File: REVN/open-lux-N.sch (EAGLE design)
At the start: 71 parts, among them IC2 MCP73831, IC3 ATMEGA32U4-AU, IC4 MCP1700-33, J2 EG1206, Q1 BSS123, Q4 BSS123, T1 FDN340P, T2 FDN340P, X2 USBSMD, X3 8MHz

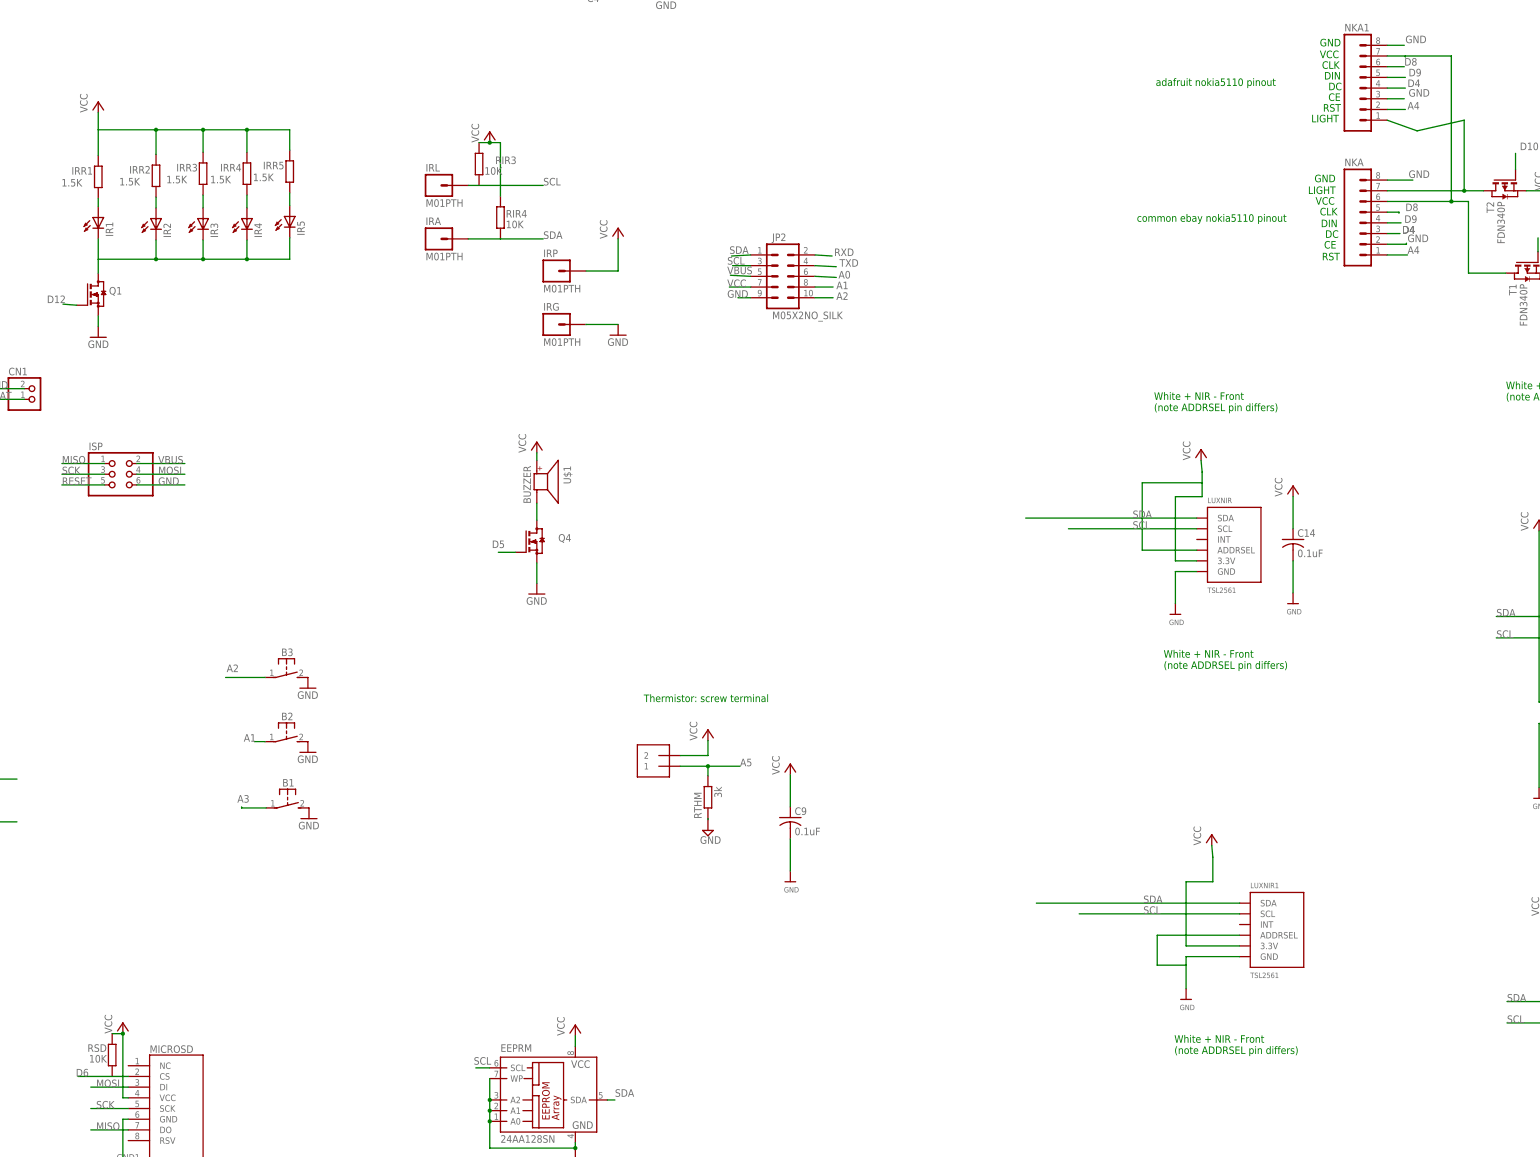
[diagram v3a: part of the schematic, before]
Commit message: fully routed
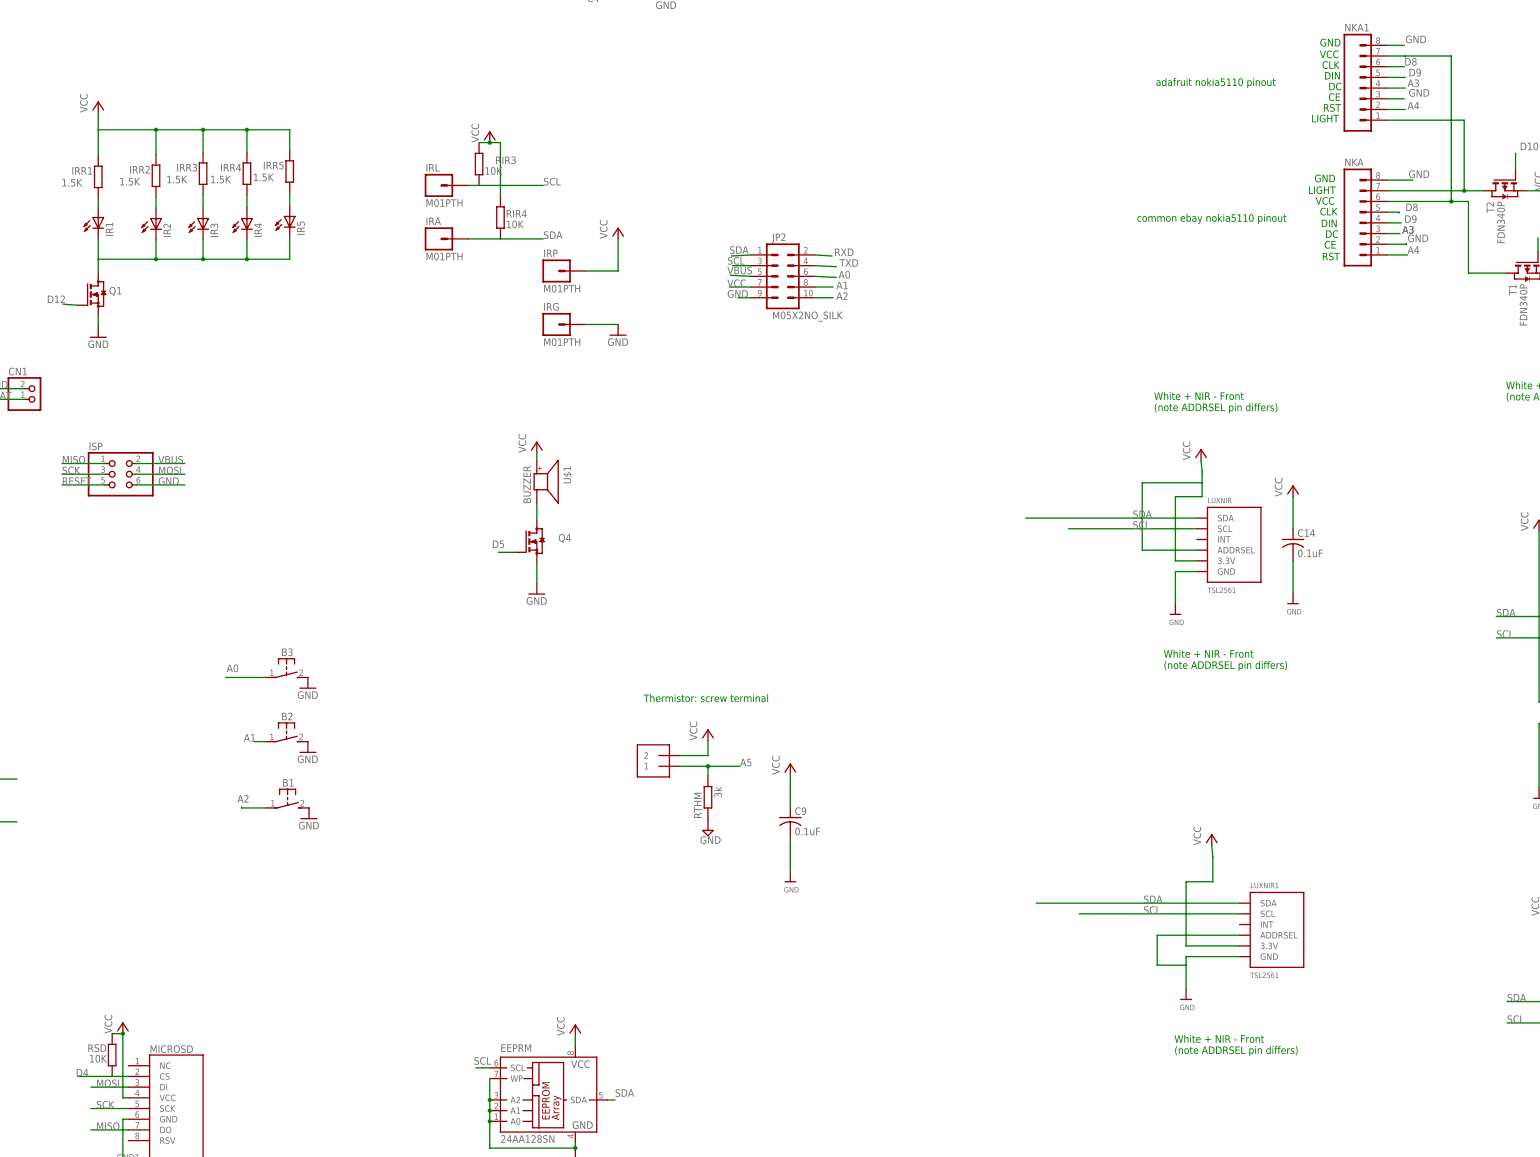
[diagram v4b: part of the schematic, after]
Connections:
- net A0: now also B3.P
- net A2: now also B1.P; no longer B3.P
- net A3: now also NKA.3, NKA1.4; no longer B1.P
- net D4: now also MICROSD.CS, RSD.1; no longer NKA.3, NKA1.4
- net D6: no longer MICROSD.CS, RSD.1
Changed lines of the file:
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@@
 <pinref part="JP2" gate="G$1" pin="6"/>
+</segment>
+<segment>
+<pinref part="B3" gate="1" pin="P"/>
+<wire x1="157.48" y1="25.4" x2="148.082" y2="25.4" width="0.1524" layer="91"/>
+<label x="148.336" y="26.67" size="1.778" layer="95"/>
 </segment>
 </net>
@@
 </segment>
 <segment>
-<pinref part="B3" gate="1" pin="P"/>
-<wire x1="157.48" y1="25.4" x2="148.082" y2="25.4" width="0.1524" layer="91"/>
-<label x="148.336" y="26.67" size="1.778" layer="95"/>
+<pinref part="B1" gate="1" pin="P"/>
+<wire x1="157.734" y1="-5.588" x2="151.892" y2="-5.588" width="0.1524" layer="91"/>
+<wire x1="151.892" y1="-5.588" x2="151.892" y2="-5.334" width="0.1524" layer="91"/>
+<label x="150.876" y="-4.318" size="1.778" layer="95"/>
 </segment>
 </net>
@@
 </segment>
 <segment>
-<pinref part="B1" gate="1" pin="P"/>
-<wire x1="157.734" y1="-5.588" x2="151.892" y2="-5.588" width="0.1524" layer="91"/>
-<wire x1="151.892" y1="-5.588" x2="151.892" y2="-5.334" width="0.1524" layer="91"/>
-<label x="150.876" y="-4.318" size="1.778" layer="95"/>
-</segment>
-</net>
-<net name="D4" class="0">
-<segment>
-<pinref part="IC3" gate="G$1" pin="PD4(ICP1/ADC8)"/>
-<wire x1="73.152" y1="-11.43" x2="76.708" y2="-11.43" width="0.1524" layer="91"/>
-<label x="76.962" y="-10.922" size="1.778" layer="95"/>
+<label x="428.752" y="165.608" size="1.778" layer="95"/>
+<pinref part="NKA1" gate="G$1" pin="4"/>
+<wire x1="423.926" y1="165.354" x2="428.244" y2="165.354" width="0.1524" layer="91"/>
 </segment>
 <segment>
@@
 <label x="427.482" y="130.81" size="1.778" layer="95"/>
 </segment>
-<segment>
-<label x="428.752" y="165.608" size="1.778" layer="95"/>
-<pinref part="NKA1" gate="G$1" pin="4"/>
-<wire x1="423.926" y1="165.354" x2="428.244" y2="165.354" width="0.1524" layer="91"/>
-</segment>
-</net>
-<net name="D8" class="0">
-<segment>
-<pinref part="IC3" gate="G$1" pin="PB4(ADC11)"/>
-<wire x1="73.152" y1="11.43" x2="78.994" y2="11.43" width="0.1524" layer="91"/>
-<label x="79.248" y="11.684" size="1.778" layer="95"/>
-</segment>
-<segment>
-<wire x1="423.926" y1="135.89" x2="426.72" y2="135.89" width="0.1524" layer="91"/>
-<wire x1="426.72" y1="135.89" x2="426.72" y2="135.636" width="0.1524" layer="91"/>
-<label x="428.244" y="136.144" size="1.778" layer="95"/>
-<pinref part="NKA" gate="G$1" pin="5"/>
-</segment>
-<segment>
-<pinref part="NKA1" gate="G$1" pin="6"/>
-<wire x1="423.926" y1="170.434" x2="427.99" y2="170.434" width="0.1524" layer="91"/>
-<label x="427.99" y="170.688" size="1.778" layer="95"/>
-</segment>
-</net>
-<net name="D5" class="0">
-<segment>
-<wire x1="73.152" y1="26.67" x2="80.772" y2="26.67" width="0.1524" layer="91"/>
-<label x="75.692" y="26.67" size="1.778" layer="95"/>
-<pinref part="IC3" gate="G$1" pin="PC6(OC1A)"/>
-</segment>
-<segment>
-<pinref part="Q4" gate="G$1" pin="G"/>
-<wire x1="216.916" y1="55.118" x2="212.852" y2="55.118" width="0.1524" layer="91"/>
-<label x="211.328" y="56.134" size="1.778" layer="95"/>
-</segment>
-</net>
-<net name="D6" class="0">
-<segment>
-<wire x1="85.852" y1="-3.81" x2="73.152" y2="-3.81" width="0.1524" layer="91"/>
-<label x="75.692" y="-3.81" size="1.778" layer="95"/>
-<pinref part="IC3" gate="G$1" pin="PD7(OC4D/ADC10/T0)"/>
-</segment>
-<segment>
-<pinref part="WS1" gate="G$1" pin="IN"/>
-<wire x1="252.73" y1="199.39" x2="261.366" y2="199.39" width="0.1524" layer="91"/>
-<label x="261.112" y="199.898" size="1.778" layer="95"/>
+</net>
+<net name="D4" class="0">
+<segment>
+<pinref part="IC3" gate="G$1" pin="PD4(ICP1/ADC8)"/>
+<wire x1="73.152" y1="-11.43" x2="76.708" y2="-11.43" width="0.1524" layer="91"/>
+<label x="76.962" y="-10.922" size="1.778" layer="95"/>
 </segment>
 <segment>
@@
 <wire x1="121.158" y1="-69.342" x2="113.03" y2="-69.342" width="0.1524" layer="91"/>
 <label x="112.522" y="-69.342" size="1.778" layer="95"/>
+</segment>
+</net>
+<net name="D8" class="0">
+<segment>
+<pinref part="IC3" gate="G$1" pin="PB4(ADC11)"/>
+<wire x1="73.152" y1="11.43" x2="78.994" y2="11.43" width="0.1524" layer="91"/>
+<label x="79.248" y="11.684" size="1.778" layer="95"/>
+</segment>
+<segment>
+<wire x1="423.926" y1="135.89" x2="426.72" y2="135.89" width="0.1524" layer="91"/>
+<wire x1="426.72" y1="135.89" x2="426.72" y2="135.636" width="0.1524" layer="91"/>
+<label x="428.244" y="136.144" size="1.778" layer="95"/>
+<pinref part="NKA" gate="G$1" pin="5"/>
+</segment>
+<segment>
+<pinref part="NKA1" gate="G$1" pin="6"/>
+<wire x1="423.926" y1="170.434" x2="427.99" y2="170.434" width="0.1524" layer="91"/>
+<label x="427.99" y="170.688" size="1.778" layer="95"/>
+</segment>
+</net>
+<net name="D5" class="0">
+<segment>
+<wire x1="73.152" y1="26.67" x2="80.772" y2="26.67" width="0.1524" layer="91"/>
+<label x="75.692" y="26.67" size="1.778" layer="95"/>
+<pinref part="IC3" gate="G$1" pin="PC6(OC1A)"/>
+</segment>
+<segment>
+<pinref part="Q4" gate="G$1" pin="G"/>
+<wire x1="216.916" y1="55.118" x2="212.852" y2="55.118" width="0.1524" layer="91"/>
+<label x="211.328" y="56.134" size="1.778" layer="95"/>
+</segment>
+</net>
+<net name="D6" class="0">
+<segment>
+<wire x1="85.852" y1="-3.81" x2="73.152" y2="-3.81" width="0.1524" layer="91"/>
+<label x="75.692" y="-3.81" size="1.778" layer="95"/>
+<pinref part="IC3" gate="G$1" pin="PD7(OC4D/ADC10/T0)"/>
+</segment>
+<segment>
+<pinref part="WS1" gate="G$1" pin="IN"/>
+<wire x1="252.73" y1="199.39" x2="261.366" y2="199.39" width="0.1524" layer="91"/>
+<label x="261.112" y="199.898" size="1.778" layer="95"/>
 </segment>
 </net>
@@
 <segment>
 <pinref part="NKA1" gate="G$1" pin="1"/>
-<wire x1="423.926" y1="157.734" x2="431.038" y2="155.194" width="0.1524" layer="91"/>
+<wire x1="423.926" y1="157.734" x2="442.214" y2="157.734" width="0.1524" layer="91"/>
 <wire x1="423.926" y1="140.97" x2="442.214" y2="140.97" width="0.1524" layer="91"/>
 <pinref part="T2" gate="A" pin="D"/>
 <pinref part="NKA" gate="G$1" pin="7"/>
 <wire x1="442.214" y1="140.97" x2="446.786" y2="140.97" width="0.1524" layer="91"/>
-<wire x1="431.038" y1="155.194" x2="442.214" y2="157.734" width="0.1524" layer="91"/>
 <wire x1="442.214" y1="157.734" x2="442.214" y2="140.97" width="0.1524" layer="91"/>
 <junction x="442.214" y="140.97"/>

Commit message: update
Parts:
- renumbered CN1 to JST, R-BTN to RESET
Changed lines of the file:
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@@
 <part name="RC" library="rcl" deviceset="R-EU_" device="R0805" value="22K"/>
 <part name="BAT1" library="SparkFunNew" deviceset="BATTERY" device="BATTCOM_20MM_PTH_SMT" value="LIR2032"/>
-<part name="CN1" library="adafruit" deviceset="JST_2PIN" device="-SMT-RA"/>
+<part name="JST" library="adafruit" deviceset="JST_2PIN" device="-SMT-RA"/>
 <part name="IC4" library="adafruit" deviceset="MCP1700" device="SOT233" value="MCP1700-33"/>
 <part name="C3" library="resistor" deviceset="C-EU" device="C0805" value="10u"/>
@@
 <part name="GND15" library="supply1" deviceset="GND" device=""/>
 <part name="GND16" library="supply1" deviceset="GND" device=""/>
-<part name="R-BTN" library="adafruit" deviceset="EVQQ2" device="" value=""/>
+<part name="RESET" library="adafruit" deviceset="EVQQ2" device="" value=""/>
 <part name="P+16" library="supply1" deviceset="VCC" device=""/>
 <part name="P+17" library="supply1" deviceset="VCC" device=""/>
@@
 <attribute name="VALUE" x="35.56" y="97.79" size="1.778" layer="96"/>
 </instance>
-<instance part="CN1" gate="G$1" x="102.87" y="91.44"/>
+<instance part="JST" gate="G$1" x="102.87" y="91.44"/>
 <instance part="IC4" gate="1" x="64.77" y="113.03" smashed="yes">
 <attribute name="NAME" x="62.23" y="119.38" size="1.778" layer="95"/>
@@
 <instance part="GND15" gate="1" x="90.932" y="34.29" rot="MR270"/>
 <instance part="GND16" gate="1" x="7.112" y="65.024"/>
-<instance part="R-BTN" gate="G$1" x="12.192" y="70.104" rot="R270"/>
+<instance part="RESET" gate="G$1" x="12.192" y="70.104" rot="R270"/>
 <instance part="P+16" gate="VCC" x="12.192" y="41.91"/>
 <instance part="P+17" gate="VCC" x="12.192" y="18.796"/>
@@
 <net name="GND" class="0">
 <segment>
-<pinref part="CN1" gate="G$1" pin="1"/>
+<pinref part="JST" gate="G$1" pin="1"/>
 <wire x1="100.33" y1="93.98" x2="91.44" y2="93.98" width="0.1524" layer="91"/>
 <label x="91.44" y="93.98" size="1.778" layer="95"/>
@@
 <junction x="7.112" y="67.564"/>
 <pinref part="GND16" gate="1" pin="GND"/>
-<pinref part="R-BTN" gate="G$1" pin="P1"/>
-<pinref part="R-BTN" gate="G$1" pin="P"/>
+<pinref part="RESET" gate="G$1" pin="P1"/>
+<pinref part="RESET" gate="G$1" pin="P"/>
 </segment>
 <segment>
@@
 </segment>
 <segment>
-<pinref part="CN1" gate="G$1" pin="2"/>
+<pinref part="JST" gate="G$1" pin="2"/>
 <wire x1="100.33" y1="91.44" x2="91.44" y2="91.44" width="0.1524" layer="91"/>
 <label x="91.44" y="91.44" size="1.778" layer="95"/>
@@
 <wire x1="17.272" y1="52.07" x2="17.272" y2="67.564" width="0.1524" layer="91"/>
 <junction x="17.272" y="52.07"/>
-<pinref part="R-BTN" gate="G$1" pin="S"/>
-<pinref part="R-BTN" gate="G$1" pin="S1"/>
+<pinref part="RESET" gate="G$1" pin="S"/>
+<pinref part="RESET" gate="G$1" pin="S1"/>
 <wire x1="17.272" y1="70.104" x2="17.272" y2="67.564" width="0.1524" layer="91"/>
 <junction x="17.272" y="67.564"/>

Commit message: update
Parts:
- renumbered RESET to RST
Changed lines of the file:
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@@
 <part name="GND15" library="supply1" deviceset="GND" device=""/>
 <part name="GND16" library="supply1" deviceset="GND" device=""/>
-<part name="RESET" library="adafruit" deviceset="EVQQ2" device="" value=""/>
+<part name="RST" library="adafruit" deviceset="EVQQ2" device="" value=""/>
 <part name="P+16" library="supply1" deviceset="VCC" device=""/>
 <part name="P+17" library="supply1" deviceset="VCC" device=""/>
@@
 <instance part="GND15" gate="1" x="90.932" y="34.29" rot="MR270"/>
 <instance part="GND16" gate="1" x="7.112" y="65.024"/>
-<instance part="RESET" gate="G$1" x="12.192" y="70.104" rot="R270"/>
+<instance part="RST" gate="G$1" x="12.192" y="70.104" rot="R270"/>
 <instance part="P+16" gate="VCC" x="12.192" y="41.91"/>
 <instance part="P+17" gate="VCC" x="12.192" y="18.796"/>
@@
 <junction x="7.112" y="67.564"/>
 <pinref part="GND16" gate="1" pin="GND"/>
-<pinref part="RESET" gate="G$1" pin="P1"/>
-<pinref part="RESET" gate="G$1" pin="P"/>
+<pinref part="RST" gate="G$1" pin="P1"/>
+<pinref part="RST" gate="G$1" pin="P"/>
 </segment>
 <segment>
@@
 <wire x1="17.272" y1="52.07" x2="17.272" y2="67.564" width="0.1524" layer="91"/>
 <junction x="17.272" y="52.07"/>
-<pinref part="RESET" gate="G$1" pin="S"/>
-<pinref part="RESET" gate="G$1" pin="S1"/>
+<pinref part="RST" gate="G$1" pin="S"/>
+<pinref part="RST" gate="G$1" pin="S1"/>
 <wire x1="17.272" y1="70.104" x2="17.272" y2="67.564" width="0.1524" layer="91"/>
 <junction x="17.272" y="67.564"/>
